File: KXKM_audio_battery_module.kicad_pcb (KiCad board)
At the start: 2 copper layers, 73 parts, among them J1 Conn_01x06, J10 Conn_01x02, J11 Conn_01x02, J12 Audio-Jack-3, J2 TEST_1P, J3 mikroBUS_socket, J4 Conn_01x04, J5 Micro_SD_Card, J6 Conn_01x03, J7 Conn_01x04, J8 Conn_01x02, J9 Conn_01x02, P1 TC_SWD, Q1 DMN63D8LDW, Q2 DMN63D8LDW, Q3 DMN63D8LDW, SW1 SW_Push, SW2 SW_Push, SW3 SW_Push, SW4 SW_SP3T, U1 ESP32-WROOM, U2 SP3485CN, U3 MCP16331T-E/CH, U4 BTS50080-1TEA, U5 DC_DC_POL, U6 PCM5141, U7 STM32F030F4Px

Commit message: Component placement WIP - multiple Hammond enclosures drawn
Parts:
- removed J9: Conn_01x02, Connectors_TestPoints:Test_Point_2Pads_Pitch2.54mm_Drill0.8mm
- J5: moved to F.Cu
- MK1, MK2: footprint Mounting_Holes:MountingHole_3.2mm_M3 -> Mounting_Holes:MountingHole_2.5mm
- SW3: footprint Buttons_Switches_THT:SW_Tactile_SPST_Angled_PTS645Vx58-2LFS -> tom_kicad_lib:SW_Tactile_SPST_Angled_PTS645Vx58-2LFS_horiz_pads
- moved MK1 130.1 mm to (66.0, 141.0)
- moved C10 128.0 mm to (63.0, 73.8)
- moved C4 128.0 mm to (56.8, 68.0)
- moved C5 128.0 mm to (59.2, 68.0)
- moved C7 128.0 mm to (62.0, 61.8)
- moved C8 128.0 mm to (62.2, 59.0)
- moved C9 128.0 mm to (63.0, 71.8)
- moved D1 128.0 mm to (55.5, 63.6)
- moved D2 128.0 mm to (52.5, 63.2)
- moved D3 128.0 mm to (63.0, 67.0)
- moved D4 128.0 mm to (64.5, 61.8)
- moved L1 128.0 mm to (69.0, 67.8)
- moved R10 128.0 mm to (58.5, 59.5)
- moved R8 128.0 mm to (50.2, 63.8)
- moved R9 128.0 mm to (60.0, 59.5)
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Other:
- board outline added: 229.1 x 223.4 mm
- net class Default: clearance 0.2 -> 0.16; trace_width 0.2 -> 0.16
- rule trace_clearance: 0.2 -> 0.16
- rule trace_min: 0.2 -> 0.16
- board text added: "1551CBK"
- board text added: "1551JFL"
- board text added: "1551LFL"
- board text added: "1551RBK"
- board text added: "1593K"
- board text added: "1593K/L/X"
- board text added: "1593L : 2 screw"
- board text added: "Avail. height : 4.5mm bottom ; 15mm top"
- board text added: "Connecteurs ext"
- board text added: "Connecteurs int / ext"
- board text added: "ToDO : M3 mounting holes"
- board text added: "ToDo : SW3 dual footprint right angle / vertical"
- board text added: "Top : capacitor, ESP module, (SD card slot), connectors, switches, DC DC /!\ standoffs on the bottom"

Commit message: Almost all components placed... Saving before mirroring everything
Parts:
- removed BAR1: DOT-BAR, Displays:HDSP-48xx
- removed J11: Conn_01x02, Connectors_Terminal_Blocks:TerminalBlock_Pheonix_PT-3.5mm_2pol
- added C25: 10uF 50V, Capacitors_SMD:C_1206, F.Cu at (145.5, 141.5)
- added D10: Red, LEDs:LED_0603, F.Cu at (154.9, 81.8)
- added D5: Green, LEDs:LED_0603, F.Cu at (140.4, 81.8)
- added D6: Green, LEDs:LED_0603, F.Cu at (143.3, 81.8)
- added D7: Green, LEDs:LED_0603, F.Cu at (146.2, 81.8)
- added D8: Yellow, LEDs:LED_0603, F.Cu at (149.2, 81.8)
- added D9: Yellow, LEDs:LED_0603, F.Cu at (152.1, 81.8)
- added J9: Conn_01x05, Socket_Strips:Socket_Strip_Straight_1x05_Pitch2.54mm, F.Cu at (143.9, 136.0)
- C1, C10, C11, C12, C13, C14, C15, C16, C17, C18, C19, C2, C20, C21, C22, C23, C24, C3, C4, C5, C7, C8, C9, D1, D2, D4, JP1, L1, Q1, Q2, Q3, R10, R12, R13, R14, R15, R16, R7, R8, R9, RN1, RN2, RN3, RN4, U2, U3, U4, U6, U7: moved to B.Cu
- D3: footprint Diodes_SMD:D_SMA -> Diodes_SMD:D_SOD-123F; moved to B.Cu
- J2: footprint Connectors_TestPoints:Test_Point_Pad_d2.0mm -> Connectors_TestPoints:Test_Point_Pad_d1.5mm
- J4: footprint Socket_Strips:Socket_Strip_Straight_1x04_Pitch2.54mm -> Pin_Headers:Pin_Header_Straight_1x04_Pitch2.54mm_SMD_Pin1Left
- MK1, MK2: footprint Mounting_Holes:MountingHole_2.5mm -> Mounting_Holes:MountingHole_3.2mm_M3
- moved J6 129.3 mm to (117.0, 130.2), turned to 90 degrees
- moved Q3 125.7 mm to (103.8, 148.2)
- moved R12 124.9 mm to (103.8, 144.0)
- moved R7 117.0 mm to (121.0, 127.8), turned to 180 degrees
- moved C3 113.0 mm to (118.0, 127.8), turned to 180 degrees
- moved U2 109.9 mm to (121.0, 123.0), turned to 270 degrees
- moved U4 99.5 mm to (113.5, 103.6), turned to 90 degrees
- moved J7 98.4 mm to (124.6, 136.5), turned to 270 degrees
- moved Q2 82.0 mm to (135.8, 144.7)
- moved C1 80.3 mm to (167.8, 103.9)
- moved C2 80.3 mm to (162.5, 103.9)
- moved C18 79.7 mm to (130.7, 127.3), turned to 90 degrees
- moved J3 78.3 mm to (145.3, 99.8), turned to 270 degrees
- moved C14 77.2 mm to (133.3, 125.0)
- moved RN1 74.6 mm to (127.2, 145.0)
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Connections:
- net /Power/MAIN_OUT renamed +VSW
- net Net-(C19-Pad1) renamed /Audio/AUDIO_R
- net Net-(C20-Pad1) renamed /Audio/AUDIO_L
- J7 pad 1: +5V -> VBUS
- RN3 pad 1: +5V -> VBUS
- RN3 pad 2: +5V -> VBUS
- U7 pad 10: /Battery monitoring/LED_BAR_4 -> /Battery monitoring/LED_BAR_1
- U7 pad 7: /Battery monitoring/LED_BAR_1 -> /Battery monitoring/LED_BAR_4
- U7 pad 8: /Battery monitoring/LED_BAR_2 -> /Battery monitoring/LED_BAR_3
- U7 pad 9: /Battery monitoring/LED_BAR_3 -> /Battery monitoring/LED_BAR_2
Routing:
- net GND: track 69.5 -> 102.7 mm, vias 14 -> 8
- net +3V3: track 31.3 -> 8.06 mm
- net +VSW: track 0.00 -> 16.8 mm
- net +BATT: track 4.90 -> 17.9 mm, vias 0 -> 2
- net Net-(C7-Pad2): track 12.2 -> 0.00 mm
- net /Audio/AUDIO_L: track 5.54 -> 16.3 mm
- net Net-(C8-Pad2): track 7.16 -> 0.00 mm
- net /SPI_MOSI: track 0.00 -> 6.04 mm
- net /SPI_CS: track 0.00 -> 6.04 mm
- net (no net): track 0.00 -> 4.45 mm
- net Net-(C7-Pad1): track 3.98 -> 0.00 mm
- net /DMX_DI: track 0.00 -> 3.38 mm
- net /Audio/AUDIO_R: track 5.79 -> 8.59 mm
- net /I2S_LRCK: track 0.00 -> 2.72 mm
- net /I2S_BCK: track 0.00 -> 2.40 mm
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- added copper zone on F.Cu, net +BATT
- added copper zone on B.Cu, net +VSW
- added copper zone on B.Cu, net GND
- added copper zone on F.Cu, net GND
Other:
- board size 229.1 x 223.4 mm -> 56.5 x 57.5 mm
- board text added: "17>22 NC"
- board text added: "Top : capacitor, ESP module, (SD card slot), connectors, jack, switches, DC DC /!\ standoffs on the bottom"
- board text removed: "1551CBK"
- board text removed: "1551JFL"
- board text removed: "1551LFL"
- board text removed: "1551RBK"
- board text removed: "1593K"
- board text removed: "1593L : 2 screw"
- board text removed: "ToDO : M3 mounting holes"
- board text removed: "ToDo : SW3 dual footprint right angle / vertical"
- board text removed: "Top : capacitor, ESP module, (SD card slot), connectors, switches, DC DC /!\ standoffs on the bottom"

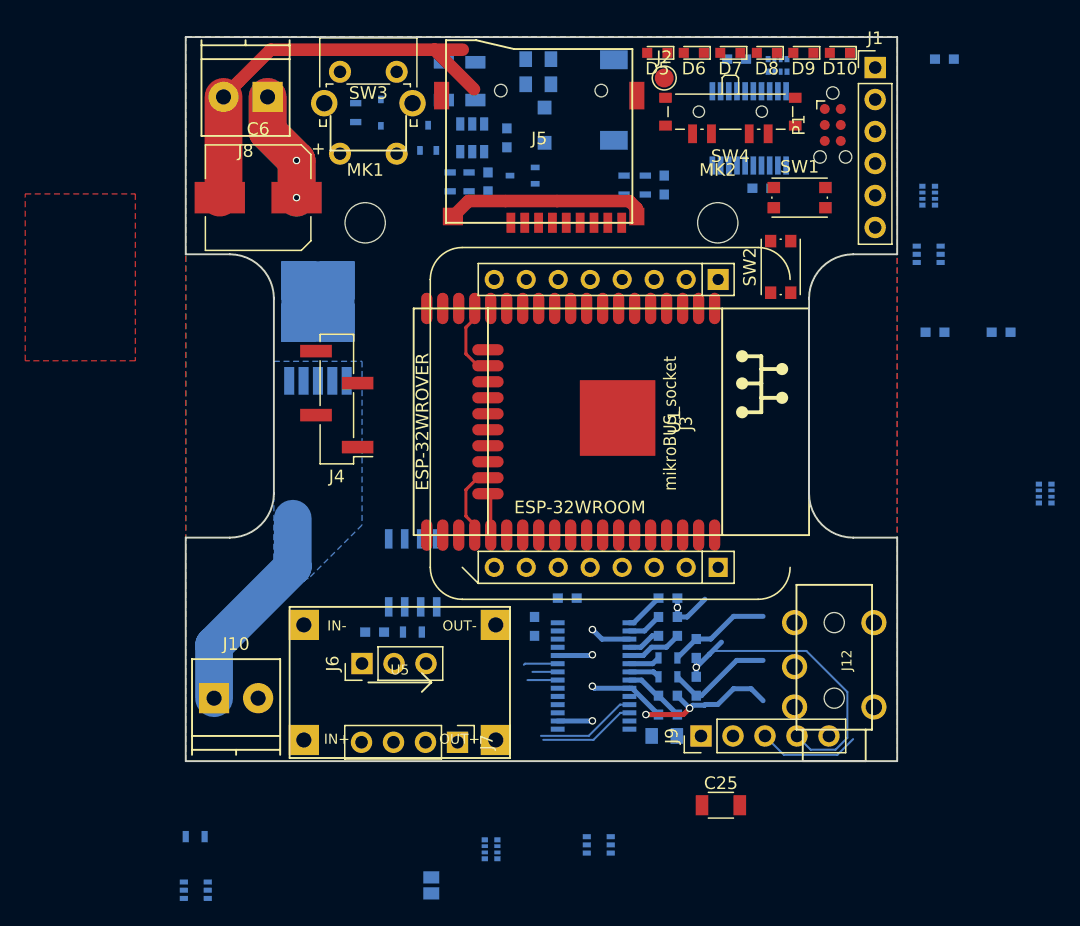
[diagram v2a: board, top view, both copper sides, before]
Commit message: v1.0   Add 3D files with Hammond enclosures  fabrication outputs
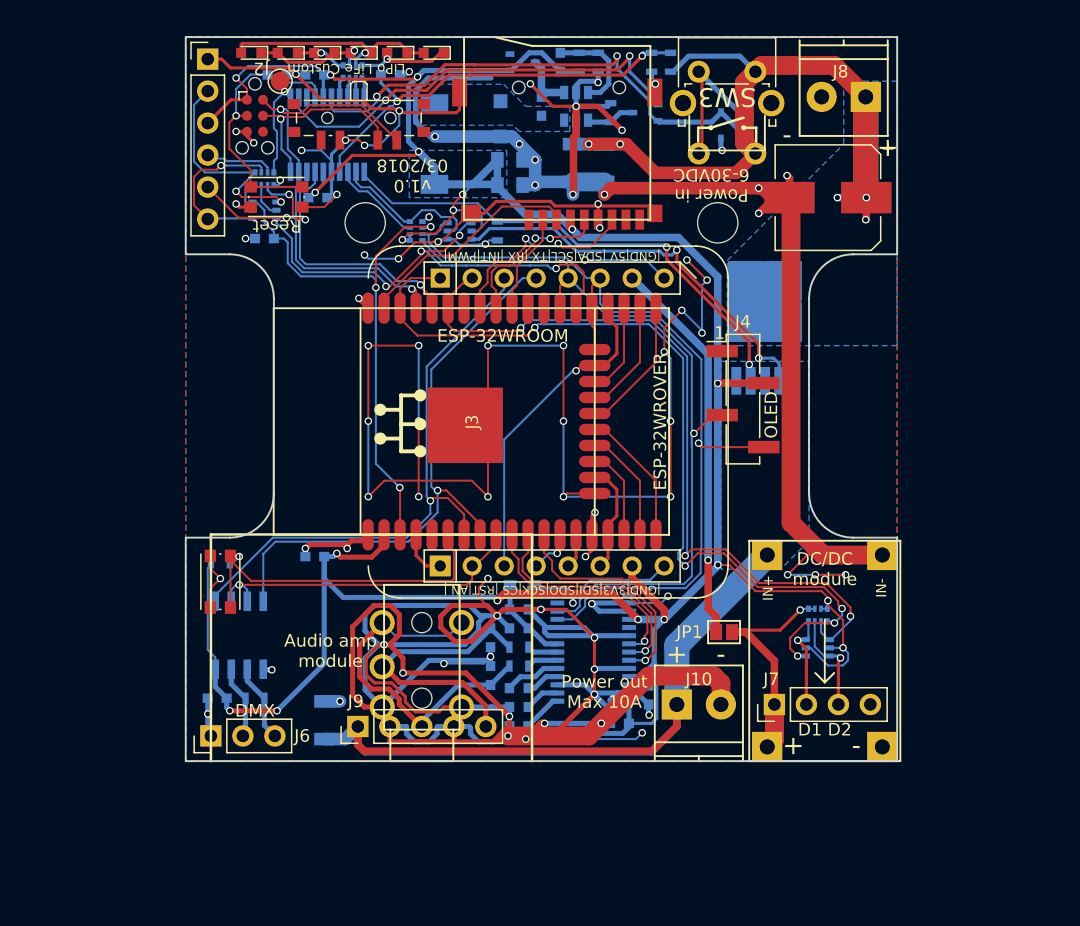
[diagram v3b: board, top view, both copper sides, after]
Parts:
- added R1: 10k, Resistors_SMD:R_0603, B.Cu at (136.8, 86.5)
- added R2: 10k, Resistors_SMD:R_0603, B.Cu at (105.8, 122.2)
- C10, C11, C9: value 10uF 10V -> 10uF,10V
- C16, C17: value 2.2uF 25V -> 2.2uF,25V
- C25: value 10uF 50V -> 10uF,50V; moved to B.Cu
- C4, C5: value 10uF 50V -> 10uF,50V
- C6: value 100uF 50V -> 100uF,50V
- D2: value Zener 3V 300mW -> Zener,3V,300mW
- D3: value 1A 60V -> 1A,60V
- J3: footprint tom_kicad_lib:MIKROBUS_HOST_CONN -> MIKROBUS_HOST_CONN
- JP1: moved to F.Cu
- L1: value 15uH 1.5A -> 15uH,1.5A
- R10: value 10k 1% -> 10k,1%
- R15: value 270k 1% -> 270k,1%
- R16, R9: value 31.6k 1% -> 31.6k,1%
- moved C1 59.0 mm to (109.2, 96.5), turned to 180 degrees
- moved Q3 56.4 mm to (124.8, 95.9)
- moved R12 53.8 mm to (127.8, 95.9), turned to 270 degrees
- moved C24 53.0 mm to (110.2, 83.5)
- moved J1 53.0 mm to (104.8, 82.2)
- moved Q1 52.9 mm to (109.2, 94.2)
- moved RN2 52.8 mm to (109.2, 91.8), turned to 270 degrees
- moved C2 52.4 mm to (113.2, 121.8), turned to 180 degrees
- moved SW2 51.0 mm to (105.8, 123.8)
- moved RN1 49.5 mm to (121.3, 95.9)
- moved J8 47.5 mm to (157.0, 85.2)
- moved P1 45.9 mm to (108.5, 86.8)
- moved C6 45.2 mm to (154.0, 93.2)
- moved SW1 41.6 mm to (110.2, 93.2)
- moved J10 36.8 mm to (142.0, 133.5)
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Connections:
- J3 pad 15: /DMX_DE -> /LED_DATA_1
- J3 pad 2: /LED_DATA_1 -> /DMX_DE
- Q3 pad 3: (no net) -> /I2C_SDA
- Q3 pad 4: (no net) -> /ESP32_BOOT
- Q3 pad 5: (no net) -> +3V3
- RN1 pad 1: /ESP32_RXI -> +3V3
- RN1 pad 3: +3V3 -> /Battery monitoring/ESP32_EN
- RN1 pad 4: /Battery monitoring/ESP32_EN -> /Battery monitoring/MAIN_OUT_EN
- RN1 pad 5: /ESP32_EN -> GND
- RN1 pad 6: /I2C_SCL -> /ESP32_EN
- RN1 pad 8: Net-(J1-Pad4) -> /I2C_SCL
- RN2 pad 1: Net-(Q1-Pad2) -> /PROG_RTS
- RN2 pad 2: Net-(Q1-Pad5) -> /PROG_DTR
- RN2 pad 3: +3V3 -> Net-(J1-Pad4)
- RN2 pad 4: +3V3 -> /Battery monitoring/STM32_BOOT
- RN2 pad 5: /LED_DATA_2 -> GND
- RN2 pad 6: /LED_DATA_1 -> /ESP32_RXI
- RN2 pad 7: /PROG_DTR -> Net-(Q1-Pad5)
- RN2 pad 8: /PROG_RTS -> Net-(Q1-Pad2)
- RN3 pad 3: /Battery monitoring/MAIN_OUT_EN -> +3V3
- RN3 pad 4: /Battery monitoring/STM32_BOOT -> +3V3
- RN3 pad 5: GND -> /LED_DATA_2
- RN3 pad 6: GND -> /LED_DATA_1
- SW3 pad : (no net) -> GND
- SW3 pad 1: +BATT -> Net-(R8-Pad1)
- SW3 pad 2: Net-(R8-Pad1) -> +BATT
- SW4 pad : (no net) -> GND
- U1 pad 10: /I2S_LRCK -> /I2S_BCK
- U1 pad 11: /I2S_BCK -> /I2S_DATA
- U1 pad 12: /DMX_DE -> /I2S_LRCK
- U1 pad 24: /DMX_DI -> /I2C_SDA
- U1 pad 26: /LED_DATA_2 -> /I2C_SCL
- U1 pad 36: /I2S_DATA -> /LED_DATA_2
- U1 pad 8: /I2C_SDA -> /DMX_DI
- U1 pad 9: /I2C_SCL -> /DMX_DE
- U7 pad 12: /Battery monitoring/ESP32_EN -> /Battery monitoring/MAIN_OUT_EN
- U7 pad 13: /Battery monitoring/3.3V_EN -> /Battery monitoring/ESP32_EN
- U7 pad 2: /Battery monitoring/MAIN_OUT_EN -> /Battery monitoring/3.3V_EN
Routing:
- net GND: track 102.7 -> 594.2 mm, vias 8 -> 85
- net +3V3: track 8.06 -> 276.8 mm, vias 0 -> 19
- net /LED_DATA_2: track 0.00 -> 70.5 mm, vias 0 -> 5
- net /I2C_SDA: track 8.05 -> 71.8 mm, vias 0 -> 1
- net /LED_DATA_1: track 0.00 -> 61.7 mm, vias 0 -> 3
- net +VSW: track 16.8 -> 77.1 mm
- net +BATT: track 17.9 -> 73.6 mm, vias 2 -> 5
- net /I2C_SCL: track 7.74 -> 62.3 mm, vias 0 -> 1
- net /DMX_RO: track 0.00 -> 46.6 mm, vias 0 -> 1
- net /ESP32_EN: track 0.00 -> 44.8 mm, vias 0 -> 3
- net /DMX_DI: track 3.38 -> 47.3 mm, vias 0 -> 1
- net /Battery monitoring/EN_PUSH_BUTTON: track 0.00 -> 40.6 mm, vias 0 -> 2
- net /Battery monitoring/LOAD_I_SENSE: track 0.00 -> 40.1 mm, vias 0 -> 2
- net /ESP32_BOOT: track 0.00 -> 38.6 mm, vias 0 -> 4
- net /Battery monitoring/3.3V_EN: track 0.00 -> 35.1 mm, vias 0 -> 2
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- added copper zone on B.Cu, net +3V3
- added copper zone on B.Cu, net +BATT
- added copper zone on B.Cu, net Net-(C7-Pad2)
- removed copper zone on F.Cu, net +BATT
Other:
- rule pad_to_mask_clearance: 0.2 -> 0.07
- board text added: "+"
- board text added: "+ -"
- board text added: "-"
- board text added: "1"
- board text added: "36/AN 33/RST 15/CS 14/SCK 12/MISO 13/MOSI +3.3V GND"
- board text added: "Audio amp module"
- board text added: "D+ D- GND"
- board text added: "D1 D2"
- board text added: "DC/DC module"
- board text added: "DMX"
- board text added: "DTR RX TX 3V3 RTS GND"
- board text added: "For +5V close JP1"
- board text added: "J2"
- board text added: "KXKM ESP32 Audio & Battery"
- board text added: "LiPo LiFe Custom"
- board text added: "OLED"
- board text added: "PWM/22 INT/21 RX/35 TX/32 SCL/4 SDA/2 +5V GND"
- board text added: "Power in 6-30VDC"
- board text added: "Power out Max 10A"
- board text added: "R GND L GND VCC"
- board text added: "Reset"
- board text added: "SW3"
- board text added: "Tom Magnier v1.0 03/2018"
- board text added: "mikroBUS"
- board text added: "v1.0 03/2018"
- board text added: "|GND|3V3|SDI|SDO|SCK|CS |RST|AN |"
- board text added: "|GND|5V |SDA|SCL|TX |RX |INT|PWM|"
- board text removed: "1593K/L/X"
- board text removed: "17>22 NC"
- board text removed: "Top : capacitor, ESP module, (SD card slot), connectors, jack, switches, DC DC /!\ standoffs on the bottom"
